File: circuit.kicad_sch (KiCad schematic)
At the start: 27 parts, among them SW101 Pedal_1, SW102 Pedal_6, SW103 Pedal_2, SW104 Pedal_7, SW105 Pedal_3, SW106 Pedal_8, SW107 Pedal_4, SW108 Program, SW109 Pedal_5, SW110 Preset, U101 ESP32-S3-DevKitC

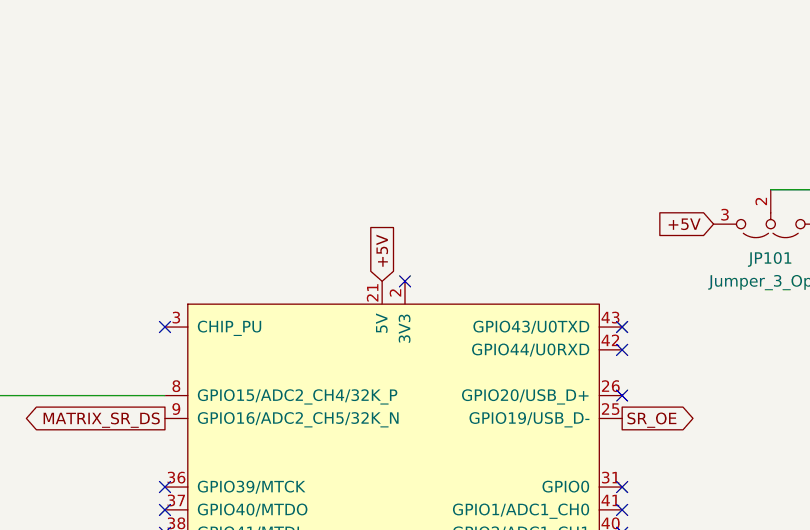
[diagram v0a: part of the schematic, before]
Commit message: New cooler (thermally) power supply.
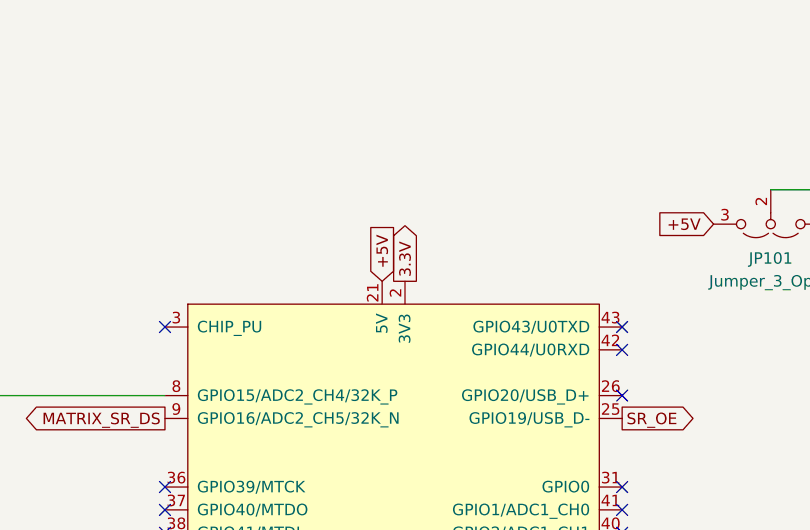
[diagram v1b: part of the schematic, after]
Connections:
- net 3.3V: now also U101.1 (3V3), U101.2 (3V3)
- no-connect marks 21 -> 20
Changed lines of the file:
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@@
-	)
-	(no_connect
-		(at 156.21 55.88)
 	)
 	(no_connect
@@
 			(effects
 				(font
+					(size 1.27 1.27)
+				)
+				(justify left)
+				(hide yes)
+			)
+		)
+	)
+	(global_label "3.3V"
+		(shape output)
+		(at 156.21 55.88 90)
+		(fields_autoplaced yes)
+		(effects
+			(font
+				(size 1.27 1.27)
+			)
+			(justify left)
+		)
+		(property "Intersheetrefs" "${INTERSHEET_REFS}"
+			(at 156.21 48.7824 90)
+			(effects
+				(font

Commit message: Removed un-needed inhibit from amp out. thereby simplifying the shift registers.
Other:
- sheet IO Routing ports: added none; removed U901_Q[0..4]
- sheet Inhibit Registers ports: added U901_Q[0..7]; removed U901_Q[0..4], U902_Q[0..3]
- sheet Pedal Routing 1 - 4 ports: added U901_Q[0..7]; removed U901_Q[0..4]
- sheet Pedal Routing 5 - 8 ports: added U901_Q[0..7]; removed U902_Q[0..3]
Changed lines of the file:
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@@
 	)
 	(junction
-		(at 363.22 255.27)
-		(diameter 0)
-		(color 0 0 0 0)
-	)
-	(junction
 		(at 299.72 139.7)
 		(diameter 0)
@@
 	)
 	(junction
+		(at 356.87 311.15)
+		(diameter 0)
+		(color 0 0 0 0)
+	)
+	(junction
 		(at 349.25 165.1)
 		(diameter 0)
@@
 		)
 	)
-	(bus
-		(pts
-			(xy 363.22 255.27) (xy 363.22 198.12)
-		)
-		(stroke
-			(width 0)
-			(type default)
-		)
-	)
 	(wire
 		(pts
@@
 		)
 	)
-	(bus
-		(pts
-			(xy 215.9 321.31) (xy 215.9 363.22)
-		)
-		(stroke
-			(width 0)
-			(type default)
-		)
-	)
 	(wire
 		(pts
@@
 		)
 	)
-	(bus
-		(pts
-			(xy 215.9 363.22) (xy 363.22 363.22)
-		)
-		(stroke
-			(width 0)
-			(type default)
-		)
-	)
 	(wire
 		(pts
@@
 		)
 	)
-	(bus
-		(pts
-			(xy 363.22 198.12) (xy 349.25 198.12)
-		)
-		(stroke
-			(width 0)
-			(type default)
-		)
-	)
-	(bus
-		(pts
-			(xy 210.82 321.31) (xy 215.9 321.31)
-		)
-		(stroke
-			(width 0)
-			(type default)
-		)
-	)
 	(wire
 		(pts
@@
 		)
 	)
-	(bus
-		(pts
-			(xy 349.25 255.27) (xy 363.22 255.27)
-		)
-		(stroke
-			(width 0)
-			(type default)
-		)
-	)
 	(wire
 		(pts
@@
 		)
 	)
-	(bus
-		(pts
-			(xy 363.22 363.22) (xy 363.22 255.27)
-		)
-		(stroke
-			(width 0)
-			(type default)
-		)
-	)
 	(wire
 		(pts
@@
 		)
 	)
+	(bus
+		(pts
+			(xy 356.87 255.27) (xy 356.87 311.15)
+		)
+		(stroke
+			(width 0)
+			(type default)
+		)
+	)
 	(wire
 		(pts
@@
 		)
 	)
+	(bus
+		(pts
+			(xy 356.87 255.27) (xy 349.25 255.27)
+		)
+		(stroke
+			(width 0)
+			(type default)
+		)
+	)
 	(wire
 		(pts
@@
 			)
 		)
-		(pin "U901_Q[0..4]" output
-			(at 210.82 321.31 0)
-			(effects
-				(font
-					(size 1.27 1.27)
-				)
-				(justify right)
-			)
-		)
-		(pin "U902_Q[0..3]" output
+		(pin "U901_Q[0..7]" output
 			(at 210.82 318.77 0)
 			(effects
@@
 			)
 		)
-		(pin "U902_Q[0..3]" output
+		(pin "U901_Q[0..7]" output
 			(at 349.25 311.15 0)
 			(effects
@@
 			)
 		)
-		(pin "U901_Q[0..4]" output
+		(pin "U901_Q[0..7]" output
 			(at 349.25 255.27 0)
 			(effects
@@
 			)
 		)
-		(pin "U701_Q[0..7]" input
+		(pin "U701_Q[0..7]" output
 			(at 237.49 198.12 180)
 			(effects
@@
 			)
 		)
-		(pin "U901_Q[0..4]" output
-			(at 349.25 198.12 0)
-			(effects
-				(font
-					(size 1.27 1.27)
-				)
-				(justify right)
-			)
-		)
